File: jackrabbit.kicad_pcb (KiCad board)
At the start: 2 copper layers, 45.1 x 29.2 mm, 64 parts, among them J1 USB_C, J2 PinHeader_2.54mm_02x10, J3 PinHeader_2.54mm_02x04, J4 PinHeader_2.54mm_01x03, SW1 SW_Push, SW2 SW_Push, U1 MIC5319-3.3YD5, U2 74LVCH245A, U3 W25Q16JVSNIQ, U4 RP2040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

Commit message: Fix pcb file for OSHpark
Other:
- board text added: "10.00 mils"
- board text added: "1775.00 mils x 1150.00 mils"
- board text added: "6.00 mils / 0.00 mils"
- board text added: "64.80 mils"
- board text added: "BOARD CHARACTERISTICS"
- board text added: "Board Thickness:"
- board text added: "Board overall dimensions:"
- board text added: "Castellated pads:"
- board text added: "Copper Finish:"
- board text added: "Copper Layer Count:"
- board text added: "ENIG"
- board text added: "Edge card connectors:"
- board text added: "Impedance Control:"
- board text added: "Min hole diameter:"
- board text added: "Min track/spacing:"
- board text added: "No"
- board text added: "Plated Board Edge:"

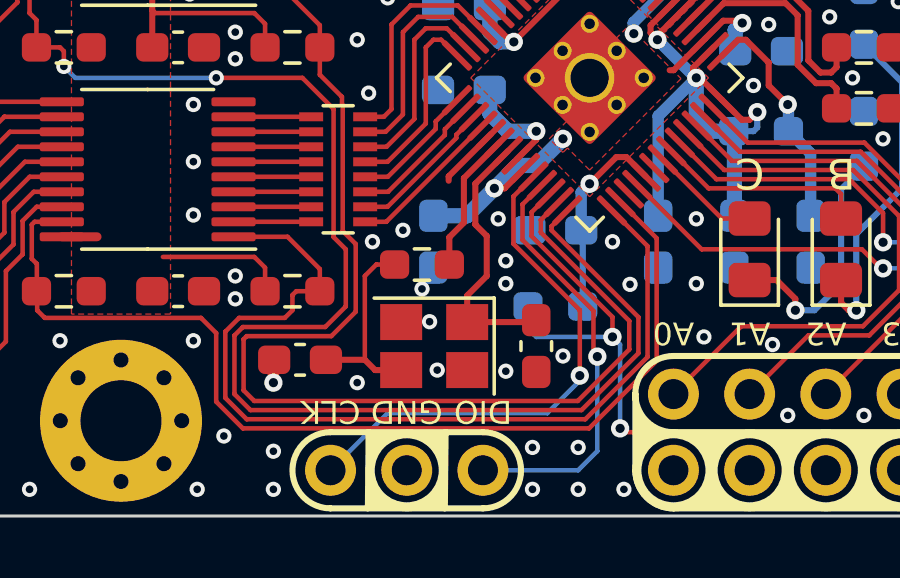
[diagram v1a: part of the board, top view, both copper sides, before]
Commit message: Make crystal footprint; check footprints
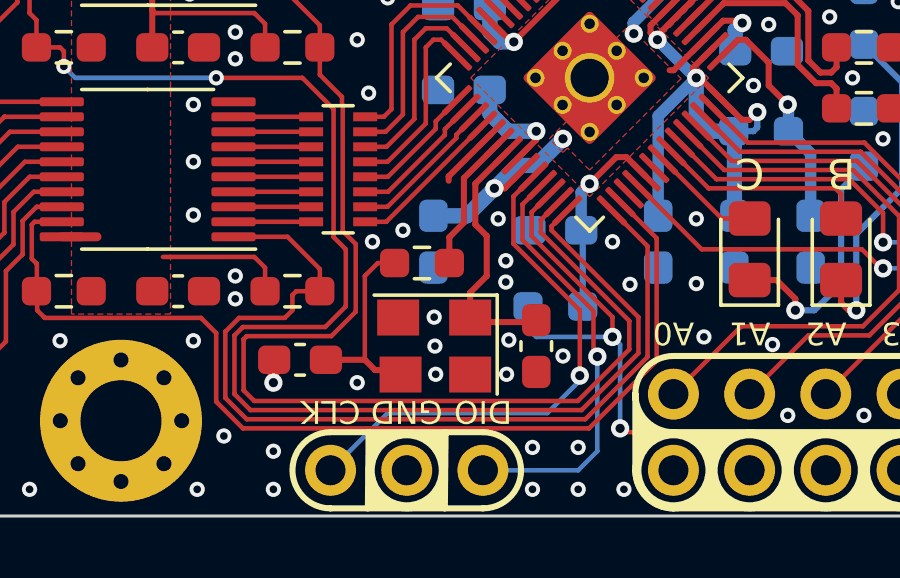
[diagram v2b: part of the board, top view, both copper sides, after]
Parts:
- Y1: footprint Crystal:Crystal_SMD_SeikoEpson_FA238-4Pin_3.2x2.5mm -> jackrabbit:Crystal_SMD_ECS-4Pin_3.2x2.5mm
- moved R10 0.05 mm to (141.3, 111.6)
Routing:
- net GND: vias 128 -> 129
